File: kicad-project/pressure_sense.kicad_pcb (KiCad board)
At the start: 2 copper layers, 71.5 x 76.9 mm, 26 parts, among them J1 Conn_02x14_Odd_Even, U1 SN74LV1T34DBV

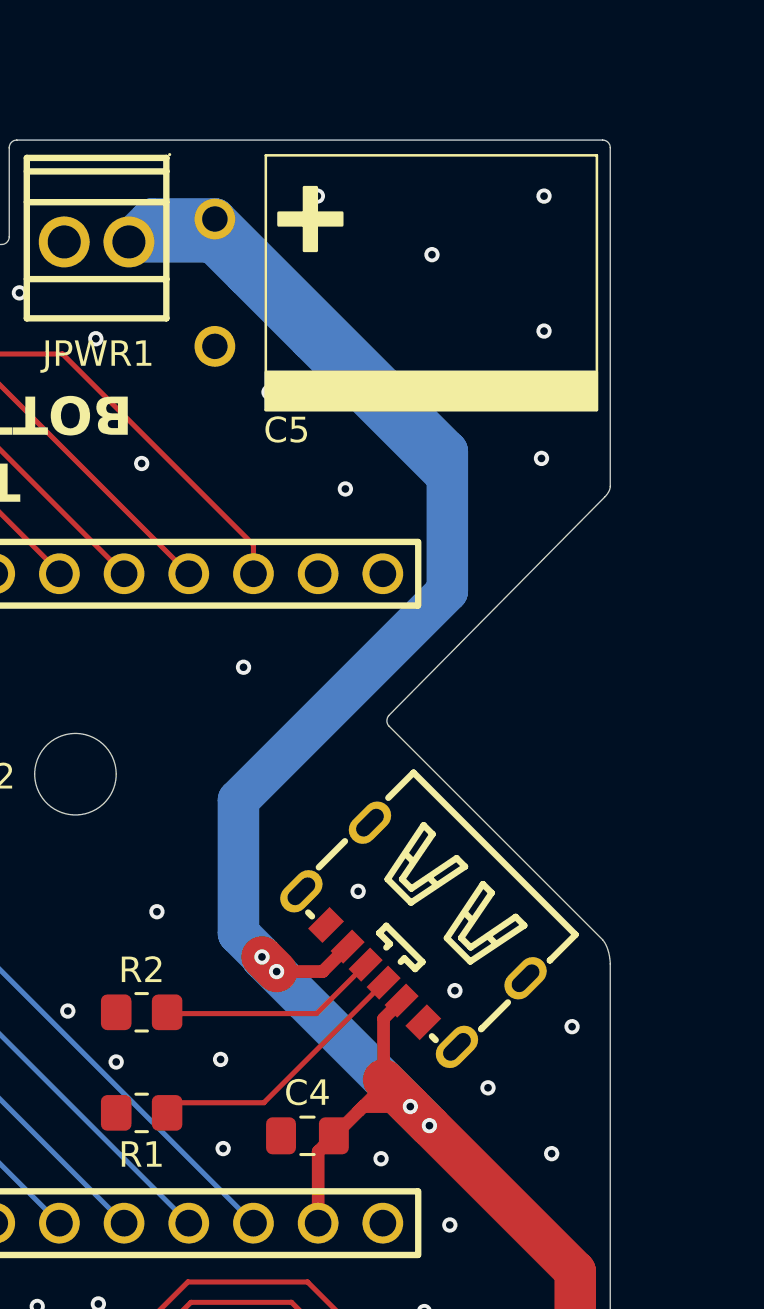
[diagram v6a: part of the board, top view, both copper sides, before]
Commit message: JLCPCB DFM check
modifications to mostly satisfy JLCPCB's DFM check
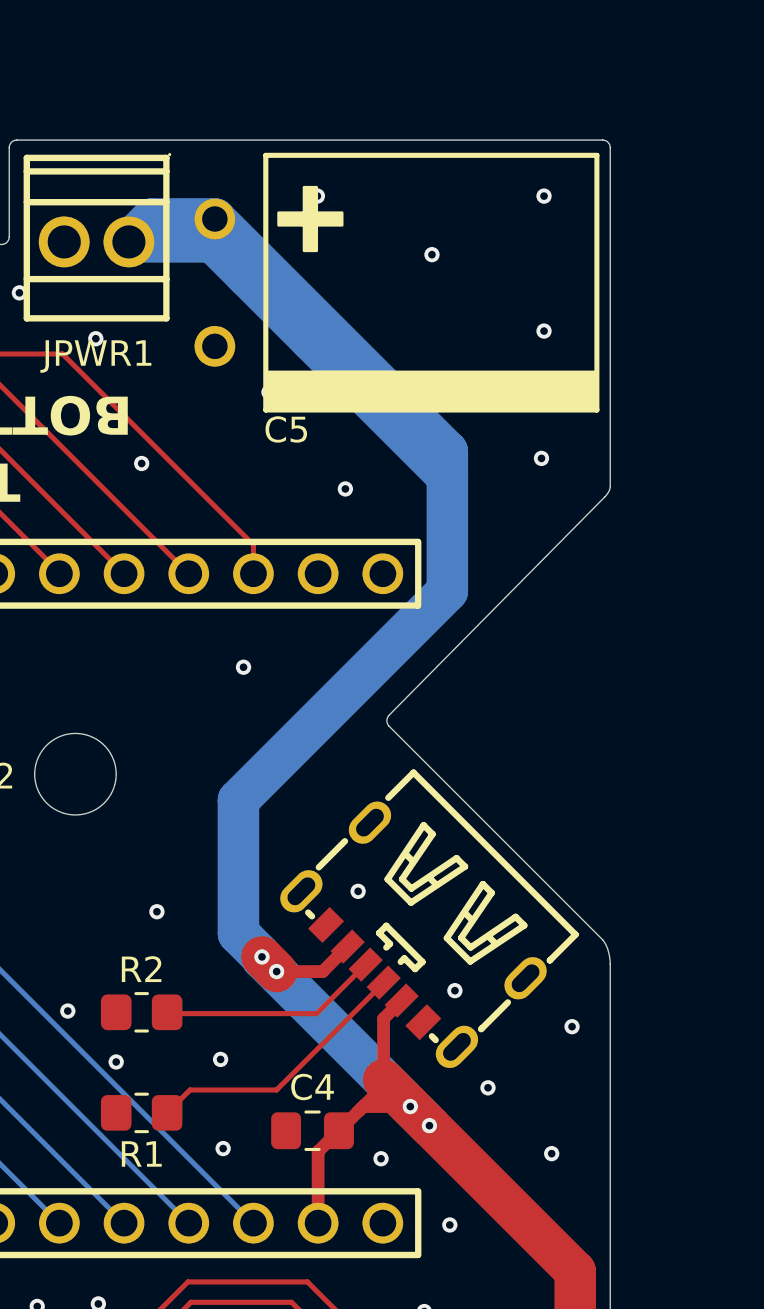
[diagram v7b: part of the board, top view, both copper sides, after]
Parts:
- moved C4 0.28 mm to (122.1, 63.6)
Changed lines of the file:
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@@
 			(sketchdnponfab yes)
 			(crossoutdnponfab yes)
-			(subtractmaskfromsilk no)
+			(subtractmaskfromsilk yes)
 			(outputformat 1)
 			(mirror no)
 			(drillshape 0)
 			(scaleselection 1)
-			(outputdirectory "output/")
+			(outputdirectory "production/")
 		)
 	)
@@
 		(sheetname "/")
 		(sheetfile "pressure_sense.kicad_sch")
-		(units
-			(unit
-				(name "A")
-				(pins "1" "3" "5" "7" "9" "11" "13" "15" "17" "19" "21" "23" "25" "27"
-					"2" "4" "6" "8" "10" "12" "14" "16" "18" "20" "22" "24" "26" "28"
-				)
-			)
-		)
 		(attr through_hole)
 		(duplicate_pad_numbers_are_jumpers no)
@@
 				(header yes)
 				(stroke
-					(width 0.1)
+					(width 0.2)
 					(type solid)
 				)
@@
 				(cols yes)
 				(stroke
-					(width 0.1)
+					(width 0.2)
 					(type solid)
 				)
@@
 		(sheetname "/")
 		(sheetfile "pressure_sense.kicad_sch")
-		(units
-			(unit
-				(name "A")
-				(pins "1" "2")
-			)
-		)
 		(attr smd)
 		(duplicate_pad_numbers_are_jumpers no)
@@
 			(end 5 -2)
 			(stroke
-				(width 0.1)
+				(width 0.2)
 				(type default)
 			)
@@
 			(end -5 -15)
 			(stroke
-				(width 0.1)
+				(width 0.2)
 				(type default)
 			)
@@
 			(end 5 -2)
 			(stroke
-				(width 0.1)
+				(width 0.2)
 				(type default)
 			)
@@
 			(end -5 -15)
 			(stroke
-				(width 0.1)
+				(width 0.2)
 				(type default)
 			)
@@
 	)
 	(footprint "Capacitor_SMD:C_0805_2012Metric_Pad1.18x1.45mm_HandSolder"
-		(locked yes)
 		(layer "F.Cu")
-		(at 121.909974 63.8)
+		(at 122.109974 63.6)
 		(descr "Capacitor SMD 0805 (2012 Metric), square (rectangular) end terminal, IPC-7351 nominal with elongated pad for handsoldering. (Body size source: IPC-SM-782 page 76, https://www.pcb-3d.com/wordpress/wp-content/uploads/ipc-sm-782a_amendment_1_and_2.pdf, https://docs.google.com/spreadsheets/d/1BsfQQcO9C6DZCsRaXUlFlo91Tg2WpOkGARC1WS5S8t0/edit?usp=sharing)")
 		(tags "capacitor handsolder")
@@
 		)
 	)
-	(gr_text "By Ayden Yak\nFor FALLOUT"
-		(at 121.3 64.2 0)
+	(gr_text "Melbourne, AUS, 2026!\n"
+		(at 97.3 47.2 0)
 		(layer "B.SilkS")
 		(effects
 			(font
 				(size 1 1)
-				(thickness 0.1)
+				(thickness 0.2)
+				(bold yes)
 			)
 			(justify left bottom mirror)
 		)
 	)
-	(gr_text "Melbourne, AUS, 2026!\n"
-		(at 77.2 48.2 55)
+	(gr_text "By Ayden Yak\nFor FALLOUT"
+		(at 121.3 64.2 0)
 		(layer "B.SilkS")
 		(effects
 			(font
 				(size 1 1)
-				(thickness 0.1)
+				(thickness 0.2)
+				(bold yes)
 			)
 			(justify left bottom mirror)
@@
 	)
 	(segment
-		(start 116.8 62.5)
-		(end 120.2 62.5)
+		(start 117.3 62)
+		(end 120.7 62)
 		(width 0.2)
 		(layer "F.Cu")
@@
 	)
 	(segment
-		(start 116.4 62.9)
-		(end 116.8 62.5)
+		(start 124.902492 57.797508)
+		(end 124.902492 57.782537)
 		(width 0.2)
 		(layer "F.Cu")
@@
 	)
 	(segment
-		(start 120.2 62.5)
+		(start 120.7 62)
 		(end 124.902492 57.797508)
 		(width 0.2)
@@
 	)
 	(segment
-		(start 124.902492 57.797508)
-		(end 124.902492 57.782537)
+		(start 116.4 62.9)
+		(end 117.3 62)
 		(width 0.2)
 		(layer "F.Cu")
